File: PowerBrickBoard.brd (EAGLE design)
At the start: 60.3 x 40 mm, 7 parts

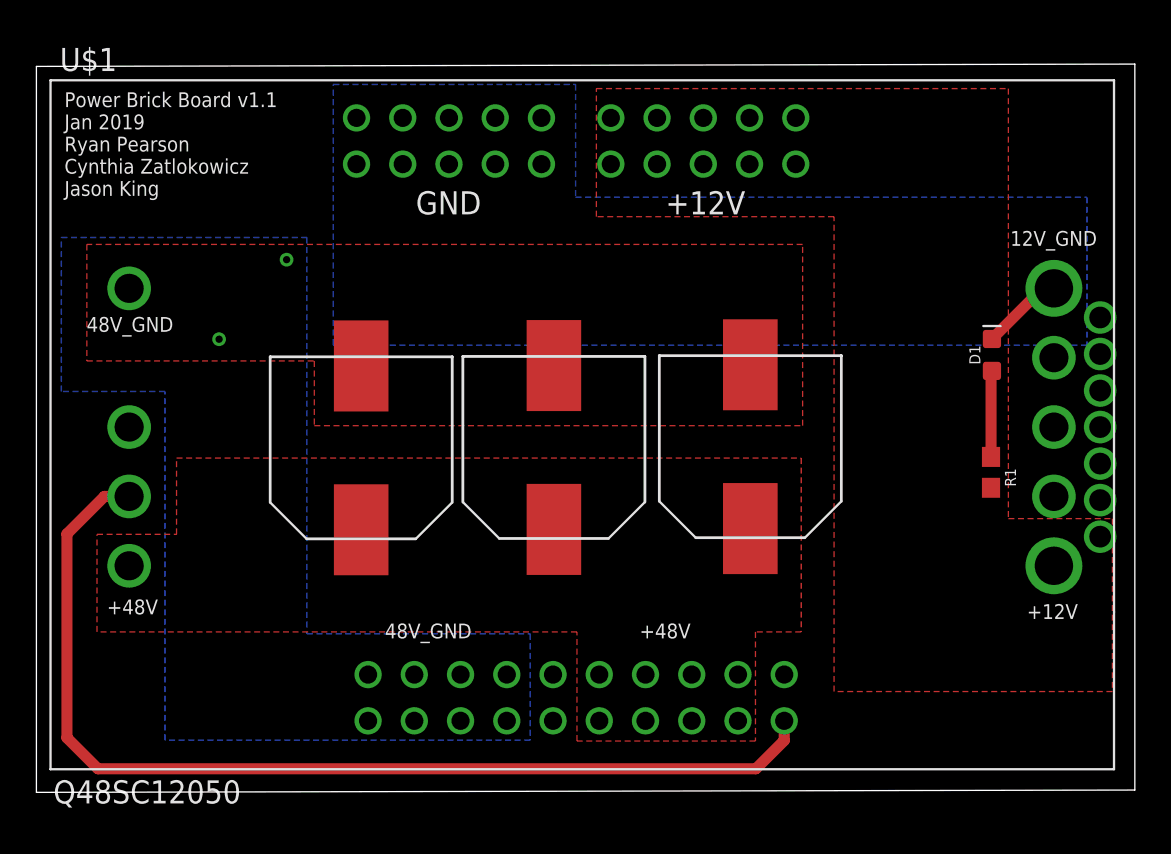
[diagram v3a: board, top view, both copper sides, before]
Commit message: updated to jasons desires
changed width sizes and corrected pin layout of on/off switch, added more vias for the overlapping polygon, moved resistor and LED to optimize the +12V polygon
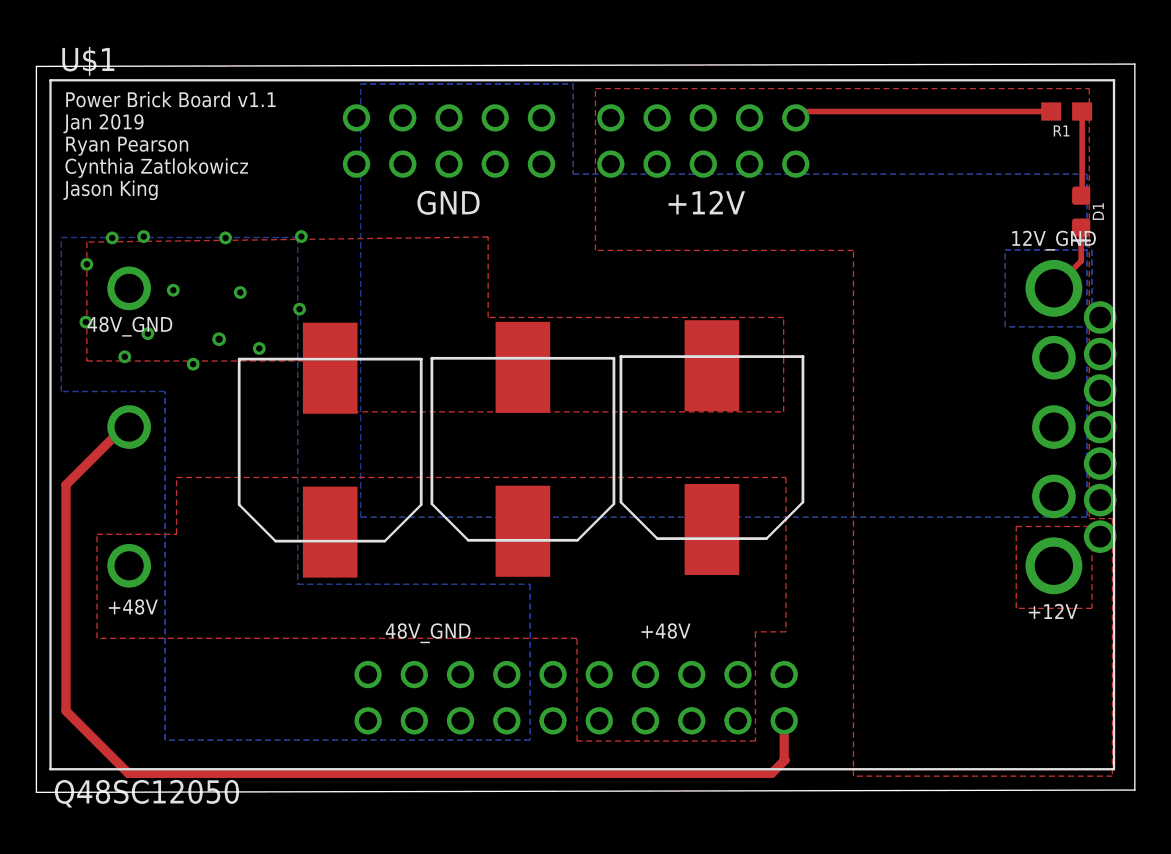
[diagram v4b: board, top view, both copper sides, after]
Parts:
- moved R1 20.3 mm to (56.6, 37.4), turned to 180 degrees
- moved D1 9.28 mm to (57.4, 31.9), turned to 270 degrees
- moved U$3 2.11 mm to (37.1, 18.9)
- moved U$5 1.71 mm to (16.1, 18.8)
- moved U$4 1.70 mm to (26.7, 18.8)
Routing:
- net +12V: track 0.00 -> 14.2 mm
- net ON/OFF: track 57.3 -> 60.6 mm
- net GND: track 4.56 -> 3.96 mm
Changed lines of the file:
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@@
 </element>
 <element name="U$2" library="PDB_TO_BRICKS" package="BRICK_TO_POWER_DIST_WHOLE" value="BRICK_TO_POWER_DIST_WHOLE" x="59.7027" y="0" rot="MR0"/>
-<element name="U$3" library="UCM1H331MNL1GS" package="UCM1H331MNL1GS" value="330 uF" x="39.2158" y="18.9889" rot="R180"/>
-<element name="U$4" library="UCM1H331MNL1GS" package="UCM1H331MNL1GS" value="330 uF" x="28.42534375" y="18.9462375" rot="R180"/>
-<element name="U$5" library="UCM1H331MNL1GS" package="UCM1H331MNL1GS" value="330 uF" x="17.8399" y="18.9254" rot="R180"/>
-<element name="D1" library="SparkFun-LED" library_urn="urn:adsk.eagle:library:529" package="LED-0603" package3d_urn="urn:adsk.eagle:package:39354/1" value="" x="52.4891" y="24.0284" rot="R90">
-<attribute name="NAME" x="51.8541" y="24.0284" size="0.6096" layer="25" font="vector" ratio="20" rot="R90" align="bottom-center"/>
-<attribute name="VALUE" x="53.1241" y="24.0284" size="0.6096" layer="27" font="vector" ratio="20" rot="R90" align="top-center"/>
+<element name="U$3" library="UCM1H331MNL1GS" package="UCM1H331MNL1GS" value="330 uF" x="37.1076" y="18.9381" rot="R180"/>
+<element name="U$4" library="UCM1H331MNL1GS" package="UCM1H331MNL1GS" value="330 uF" x="26.72354375" y="18.8446375" rot="R180"/>
+<element name="U$5" library="UCM1H331MNL1GS" package="UCM1H331MNL1GS" value="330 uF" x="16.1381" y="18.7984" rot="R180"/>
+<element name="D1" library="SparkFun-LED" library_urn="urn:adsk.eagle:library:529" package="LED-0603" package3d_urn="urn:adsk.eagle:package:39354/1" value="" x="57.3913" y="31.9024" rot="R270">
+<attribute name="NAME" x="58.0263" y="31.9024" size="0.6096" layer="25" font="vector" ratio="20" rot="R270" align="bottom-center"/>
+<attribute name="VALUE" x="56.7563" y="31.9024" size="0.6096" layer="27" font="vector" ratio="20" rot="R270" align="top-center"/>
 </element>
-<element name="R1" library="SparkFun-Resistors" library_urn="urn:adsk.eagle:library:532" package="0603" package3d_urn="urn:adsk.eagle:package:39650/1" value=" 470" x="52.4383" y="17.5768" rot="R270">
-<attribute name="NAME" x="53.2003" y="17.2974" size="0.6096" layer="25" font="vector" ratio="20" rot="R270" align="bottom-center"/>
-<attribute name="PROD_ID" value=" " x="52.4383" y="17.5768" size="1.778" layer="27" rot="R270" display="off"/>
-<attribute name="VALUE" x="51.6763" y="17.5768" size="0.6096" layer="27" font="vector" ratio="20" rot="R270" align="top-center"/>
+<element name="R1" library="SparkFun-Resistors" library_urn="urn:adsk.eagle:library:532" package="0603" package3d_urn="urn:adsk.eagle:package:39650/1" value=" 470" x="56.5912" y="37.4015" rot="R180">
+<attribute name="NAME" x="56.3118" y="36.6395" size="0.6096" layer="25" font="vector" ratio="20" rot="R180" align="bottom-center"/>
+<attribute name="PROD_ID" value=" " x="56.5912" y="37.4015" size="1.778" layer="27" rot="R180" display="off"/>
+<attribute name="VALUE" x="56.5912" y="38.1635" size="0.6096" layer="27" font="vector" ratio="20" rot="R180" align="top-center"/>
 </element>
 </elements>
@@
 <contactref element="U$2" pad="+12V8"/>
 <contactref element="R1" pad="2"/>
-<polygon width="0.6096" layer="1" isolate="0.6096" thermals="no">
-<vertex x="30.7594" y="38.6588"/>
-<vertex x="53.3908" y="38.6588"/>
-<vertex x="53.3908" y="15.0368"/>
+<polygon width="2.54" layer="1" isolate="0.889" thermals="no">
+<vertex x="30.7086" y="38.6588"/>
+<vertex x="57.8358" y="38.6588"/>
+<vertex x="57.8358" y="15.0368"/>
 <vertex x="59.1058" y="15.0368"/>
-<vertex x="59.1058" y="5.5372"/>
-<vertex x="43.815" y="5.5372"/>
-<vertex x="43.815" y="31.623"/>
-<vertex x="30.7594" y="31.623"/>
+<vertex x="59.1058" y="0.889"/>
+<vertex x="44.8818" y="0.889"/>
+<vertex x="44.8818" y="29.7688"/>
+<vertex x="30.7086" y="29.7688"/>
+</polygon>
+<wire x1="55.7412" y1="37.4015" x2="42.0642" y2="37.4015" width="0.3048" layer="1"/>
+<wire x1="42.0642" y1="37.4015" x2="41.7127" y2="37.05" width="0.3048" layer="1"/>
+<polygon width="0.1524" layer="1" isolate="0.2032" thermals="no">
+<vertex x="53.8226" y="14.605"/>
+<vertex x="57.9882" y="14.605"/>
+<vertex x="57.9882" y="10.1092"/>
+<vertex x="53.8226" y="10.1092"/>
 </polygon>
 </signal>
@@
 <contactref element="U$2" pad="+48V7"/>
 <contactref element="U$2" pad="+48V8"/>
-<polygon width="0.508" layer="1" isolate="0.6096" thermals="no">
+<polygon width="2.54" layer="1" isolate="0.889" thermals="no">
 <vertex x="3.3274" y="14.1732"/>
 <vertex x="7.6962" y="14.1732"/>
-<vertex x="7.6962" y="18.3642"/>
-<vertex x="42.0116" y="18.3642"/>
-<vertex x="42.0116" y="8.8138"/>
+<vertex x="7.6962" y="17.2974"/>
+<vertex x="41.1734" y="17.2974"/>
+<vertex x="41.1734" y="8.8138"/>
 <vertex x="39.497" y="8.8138"/>
 <vertex x="39.497" y="2.8194"/>
 <vertex x="29.6926" y="2.8194"/>
-<vertex x="29.6926" y="8.8138"/>
-<vertex x="3.3274" y="8.8138"/>
+<vertex x="29.6926" y="8.4582"/>
+<vertex x="3.3274" y="8.4582"/>
 </polygon>
 </signal>
@@
 <contactref element="U$1" pad="ON/OFF"/>
 <contactref element="U$2" pad="ON/OFF"/>
-<wire x1="1.6764" y1="14.1986" x2="1.6764" y2="2.9972" width="0.6096" layer="1"/>
-<wire x1="1.6764" y1="2.9972" x2="3.3782" y2="1.2954" width="0.6096" layer="1"/>
-<wire x1="3.3782" y1="1.2954" x2="39.5224" y2="1.2954" width="0.6096" layer="1"/>
-<wire x1="39.5224" y1="1.2954" x2="41.0777" y2="2.8507" width="0.6096" layer="1"/>
-<wire x1="41.0777" y1="2.8507" x2="41.0777" y2="3.93" width="0.6096" layer="1"/>
-<wire x1="3.7338" y1="16.256" x2="1.6764" y2="14.1986" width="0.6096" layer="1"/>
-<wire x1="5.0927" y1="16.256" x2="3.7338" y2="16.256" width="0.6096" layer="1"/>
+<wire x1="1.6256" y1="4.4704" x2="5.0546" y2="1.0414" width="0.508" layer="1"/>
+<wire x1="1.6256" y1="4.4704" x2="1.6256" y2="16.891" width="0.508" layer="1"/>
+<wire x1="1.6256" y1="16.891" x2="4.8006" y2="20.066" width="0.508" layer="1"/>
+<wire x1="4.8006" y1="20.066" x2="5.0927" y2="20.066" width="0.508" layer="1"/>
+<wire x1="40.386" y1="1.0414" x2="41.1226" y2="1.778" width="0.508" layer="1"/>
+<wire x1="41.1226" y1="1.778" x2="41.0777" y2="1.8229" width="0.508" layer="1"/>
+<wire x1="41.0777" y1="1.8229" x2="41.0777" y2="3.93" width="0.508" layer="1"/>
+<wire x1="5.0546" y1="1.0414" x2="40.386" y2="1.0414" width="0.508" layer="1"/>
 </signal>
 <signal name="GND">
@@
 <contactref element="U$1" pad="VOUT-"/>
 <contactref element="D1" pad="C"/>
-<polygon width="0.6096" layer="16" isolate="0.6096" thermals="no">
-<vertex x="16.3068" y="38.8874"/>
-<vertex x="29.6164" y="38.8874"/>
-<vertex x="29.6164" y="32.6898"/>
-<vertex x="57.7088" y="32.6898"/>
-<vertex x="57.7088" y="24.5618"/>
-<vertex x="16.3068" y="24.5618"/>
+<polygon width="2.54" layer="16" isolate="0.889" thermals="no">
+<vertex x="17.8054" y="38.9128"/>
+<vertex x="29.4894" y="38.9128"/>
+<vertex x="29.4894" y="33.9598"/>
+<vertex x="57.7088" y="33.9598"/>
+<vertex x="57.7088" y="15.113"/>
+<vertex x="17.8054" y="15.113"/>
 </polygon>
-<wire x1="55.8927" y1="27.686" x2="55.2697" y2="27.686" width="0.6096" layer="1"/>
-<wire x1="55.2697" y1="27.686" x2="52.4891" y2="24.9054" width="0.6096" layer="1"/>
+<wire x1="57.3913" y1="31.0254" x2="57.3913" y2="29.1846" width="0.3048" layer="1"/>
+<wire x1="57.3913" y1="29.1846" x2="55.8927" y2="27.686" width="0.3048" layer="1"/>
+<polygon width="0.1524" layer="16" thermals="no">
+<vertex x="53.213" y="25.5778"/>
+<vertex x="53.213" y="29.7942"/>
+<vertex x="57.9882" y="29.7942"/>
+<vertex x="57.9882" y="25.5778"/>
+</polygon>
 </signal>
 <signal name="48V_GND">
@@
 <contactref element="U$2" pad="48V_GND7"/>
 <contactref element="U$2" pad="48V_GND8"/>
-<polygon width="0.508" layer="1" isolate="0.6096" thermals="no">
+<polygon width="2.54" layer="1" isolate="1.27" thermals="no">
 <vertex x="2.7686" y="23.6982"/>
 <vertex x="15.2654" y="23.6982"/>
-<vertex x="15.2654" y="20.1422"/>
-<vertex x="42.0878" y="20.1422"/>
-<vertex x="42.0878" y="30.099"/>
-<vertex x="2.7686" y="30.099"/>
+<vertex x="15.2654" y="20.9042"/>
+<vertex x="41.0464" y="20.9042"/>
+<vertex x="41.0464" y="26.0858"/>
+<vertex x="24.8158" y="26.0858"/>
+<vertex x="24.8158" y="30.508"/>
+<vertex x="2.7686" y="30.226"/>
 </polygon>
-<polygon width="0.508" layer="16" isolate="0.6096" thermals="no">
+<polygon width="2.54" layer="16" isolate="0.889" thermals="no">
 <vertex x="1.3716" y="30.48"/>
-<vertex x="14.859" y="30.48"/>
-<vertex x="14.859" y="8.7122"/>
-<vertex x="27.1272" y="8.7122"/>
+<vertex x="14.351" y="30.48"/>
+<vertex x="14.351" y="11.43"/>
+<vertex x="27.1272" y="11.43"/>
 <vertex x="27.1272" y="2.8702"/>
 <vertex x="7.0612" y="2.8702"/>
@@
 </polygon>
 <via x="10.033" y="24.892" extent="1-16" drill="0.4"/>
-<via x="13.7414" y="29.2608" extent="1-16" drill="0.4"/>
+<via x="7.5184" y="27.5844" extent="1-16" drill="0.35"/>
+<via x="11.2014" y="27.4574" extent="1-16" drill="0.35"/>
+<via x="14.4526" y="26.543" extent="1-16" drill="0.35"/>
+<via x="12.2428" y="24.384" extent="1-16" drill="0.35"/>
+<via x="8.6106" y="23.5204" extent="1-16" drill="0.35"/>
+<via x="6.1214" y="25.1968" extent="1-16" drill="0.35"/>
+<via x="4.8514" y="23.9268" extent="1-16" drill="0.35"/>
+<via x="2.7178" y="25.8318" extent="1-16" drill="0.35"/>
+<via x="2.7686" y="29.0068" extent="1-16" drill="0.35"/>
+<via x="4.1656" y="30.4546" extent="1-16" drill="0.35"/>
+<via x="5.8928" y="30.5308" extent="1-16" drill="0.35"/>
+<via x="10.3886" y="30.4546" extent="1-16" drill="0.35"/>
+<via x="14.5542" y="30.5308" extent="1-16" drill="0.35"/>
 </signal>
 <signal name="N$1">
 <contactref element="D1" pad="A"/>
 <contactref element="R1" pad="1"/>
-<wire x1="52.4891" y1="23.1514" x2="52.4383" y2="23.1006" width="0.6096" layer="1"/>
-<wire x1="52.4383" y1="23.1006" x2="52.4383" y2="18.4268" width="0.6096" layer="1"/>
+<wire x1="57.4412" y1="37.4015" x2="57.4412" y2="32.8293" width="0.3048" layer="1"/>
+<wire x1="57.4412" y1="32.8293" x2="57.3913" y2="32.7794" width="0.3048" layer="1"/>
 </signal>
 </signals>
